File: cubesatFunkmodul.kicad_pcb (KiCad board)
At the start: 4 copper layers, 85 x 85 mm, 214 parts, among them CON11 DISCO-CON1, CON21 DISCO-CON2, Q1 SSM3J334RLFTR-ND, Q10 AO3414, Q11 MMBT5551-TP, Q12 MMBT5551-TP, Q13 MMBT5551-TP, Q14 MMBT5551-TP, Q15 MMBT5551-TP, Q16 MMBT5551-TP, Q17 AO3414, Q18 AO3414, Q2 AO3414, Q3 MMBT5551-TP, Q4 MMBT5551-TP, Q5 MMBT5551-TP, Q6 MMBT5551-TP, Q7 MMBT5551-TP, Q8 MMBT5551-TP, Q9 SSM3J334RLFTR-ND, U1 MC74HC4538A, U10 RFM23BP, U2 MAX892, U3 ATMEGA128-16AU, U4 LTC3113, U5 RFM23BP, U6 MC74HC4538A, U7 MAX892, U8 ATMEGA128-16AU, U9 LTC3113, Y1 Crystal_GND24, Y2 Crystal_GND24

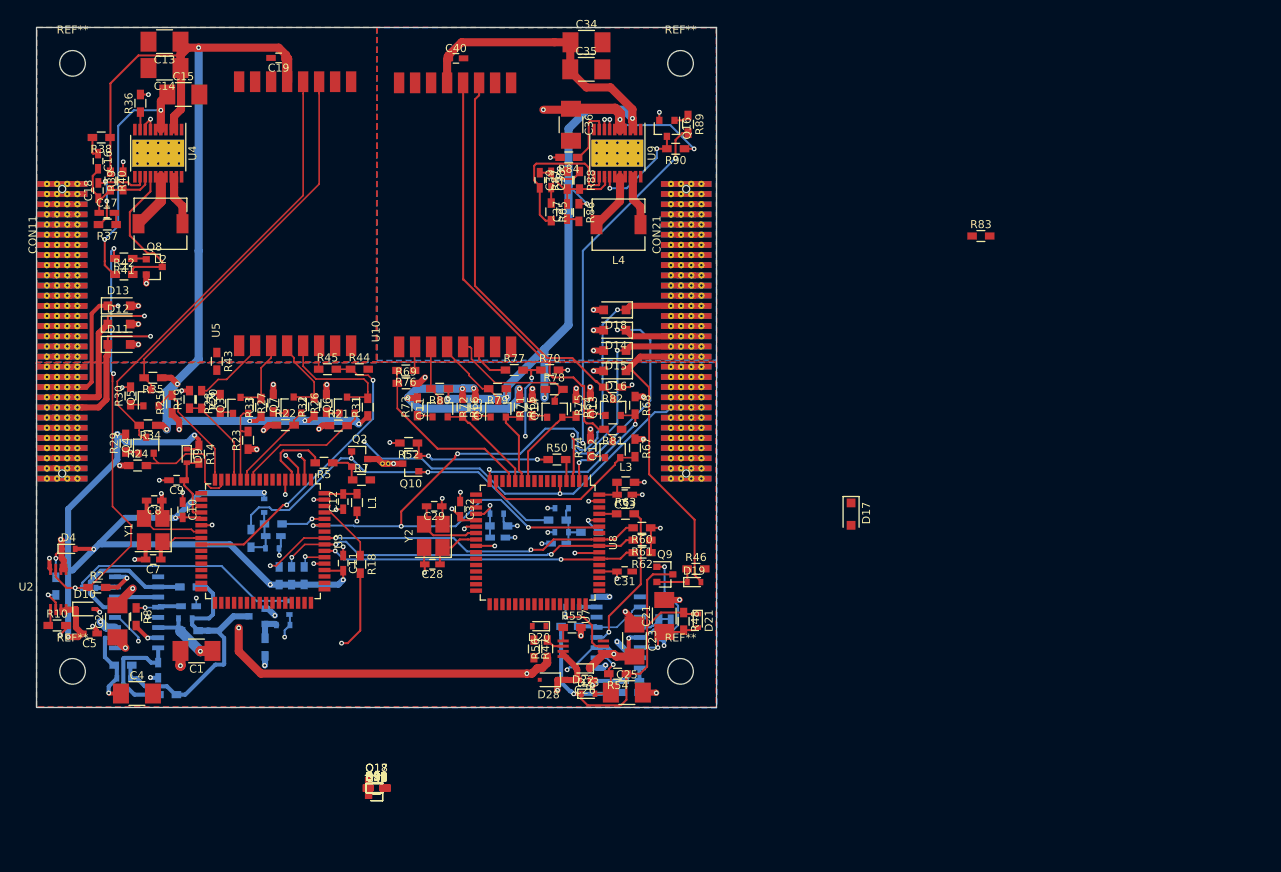
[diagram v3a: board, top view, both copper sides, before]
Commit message: Moved rf module to bottom layer
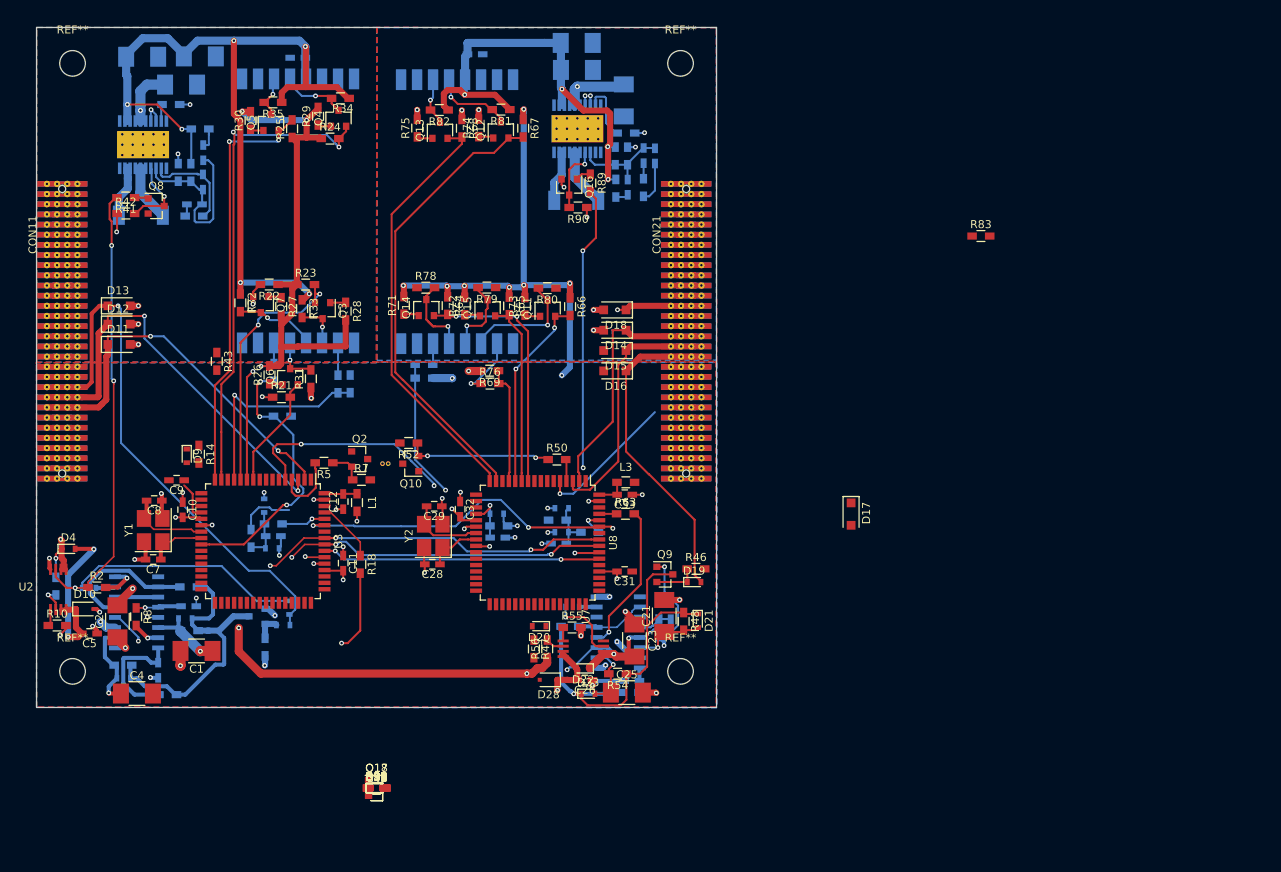
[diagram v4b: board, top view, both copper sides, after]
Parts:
- removed R15, R16, R17, R60, R61, R62: 100k, Resistors_SMD:R_0603_HandSoldering
- C13, C14, C15, C16, C17, C18, C19, C34, C35, C36, C37, C38, C39, C40, L2, L4, R19, R20, R36, R37, R38, R39, R40, R44, R45, R70, R77, R84, R85, R86, R87, R88, U10, U4, U5, U9: moved to B.Cu
- moved Q4 47.4 mm to (88.7, 45.4)
- moved R24 47.4 mm to (87.7, 47.9)
- moved R29 47.4 mm to (86.2, 45.1)
- moved R34 47.4 mm to (89.0, 42.9)
- moved Q12 42.3 mm to (109.0, 46.8)
- moved R67 42.3 mm to (111.8, 46.6)
- moved R81 42.3 mm to (109.1, 44.3)
- moved R74 42.3 mm to (106.3, 46.5)
- moved R75 40.8 mm to (98.6, 46.6)
- moved R82 40.8 mm to (101.3, 44.3)
- moved R68 40.8 mm to (104.2, 46.6)
- moved Q13 40.8 mm to (101.4, 46.9)
- moved R25 37.5 mm to (82.9, 46.7)
- moved Q5 37.5 mm to (80.3, 45.9)
- moved R30 37.5 mm to (77.8, 45.6)
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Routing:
- net /Funkmodul2/Funkeinheit2/5V: track 122.9 -> 56.1 mm, vias 7 -> 4
- net /Funkmodul1/Funkeinheit/5V: track 178.9 -> 124.6 mm, vias 6 -> 7
- net /Funkmodul1/Funkeinheit/RXON_: track 56.0 -> 8.43 mm, vias 0 -> 1
- net VBAT: track 105.1 -> 59.7 mm, vias 5 -> 4
- net /Funkmodul2/Funkeinheit2/RXON_: track 55.3 -> 10.1 mm, vias 0 -> 1
- net /Funkmodul1/Funkeinheit/RXON: track 16.0 -> 61.1 mm, vias 0 -> 2
- net /Funkmodul1/Funkeinheit/TXON_: track 49.4 -> 5.35 mm, vias 0 -> 1
- net /Funkmodul1/VCC: track 139.8 -> 96.6 mm, vias 18 -> 10
- net /Funkmodul2/Funkeinheit2/TXON_: track 48.9 -> 5.96 mm, vias 0 -> 1
- net WIRE_CONN: track 47.5 -> 7.10 mm, vias 2 -> 0
- net /Funkmodul1/Funkeinheit/TXON: track 15.0 -> 52.7 mm, vias 0 -> 2
- net /Funkmodul2/Funkeinheit2/RXON: track 21.3 -> 57.4 mm
- net /Funkmodul2/VCC: track 71.3 -> 101.2 mm, vias 17 -> 16
- net /Funkmodul2/Funkeinheit2/TXON: track 25.4 -> 53.6 mm, vias 2 -> 0
- net /Funkmodul1/Funkeinheit/MOSI: track 10.1 -> 32.8 mm, vias 0 -> 2
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
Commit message: Adds second burnwire fets
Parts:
- removed the REF** at (94.2, 88.5)
- removed the REF** at (95.0, 88.5)
- added D33: SMF3.3, Diodes_SMD:D_SOD-123F, F.Cu at (92.8, 83.7)
- C41, C42, D29, D30, D31, D32, R92, R93, R94, R96, R97, R98: moved to B.Cu
- moved D17 58.3 mm to (94.8, 89.1)
- moved R83 56.1 mm to (115.2, 75.7), turned to 270 degrees
- moved R95 48.5 mm to (95.8, 80.7)
- moved R96 47.2 mm to (95.8, 82.0), turned to 90 degrees
- moved Q17 45.9 mm to (89.7, 83.3)
- moved Q18 45.9 mm to (95.8, 83.3), turned to 180 degrees
- moved R91 45.5 mm to (85.5, 84.3), turned to 180 degrees
- moved R92 44.8 mm to (91.5, 84.3)
- moved R98 40.6 mm to (120.4, 98.7), turned to 180 degrees
- moved D31 39.5 mm to (120.5, 100.2), turned to 180 degrees
- moved D32 38.5 mm to (120.5, 101.6)
- moved C42 36.6 mm to (118.3, 102.1), turned to 270 degrees
- moved R97 34.7 mm to (115.4, 102.1), turned to 180 degrees
- moved R94 28.3 mm to (84.5, 102.3)
- moved C41 26.2 mm to (86.5, 103.8)
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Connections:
- CON21 pad 5: /Funkmodul1/TDI -> /Funkmodul2/TDI
- CON21 pad 6: /Funkmodul2/TDO -> /Funkmodul1/TDO
- R91 pad 2: /Funkmodul1/BURNWIRE -> /Funkmodul1/BURNWIRE2
- R95 pad 2: /Funkmodul2/BURNWIRE -> /Funkmodul2/BURNWIRE2
- U3 pad 55: /Funkmodul2/TDI -> /Funkmodul1/TDO
- U3 pad 6: (no net) -> /Funkmodul1/BURNWIRE2
- U8 pad 55: /Funkmodul2/TDO -> /Funkmodul1/TDI
- U8 pad 6: (no net) -> /Funkmodul2/BURNWIRE2
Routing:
- net /Funkmodul1/TDO: track 0.00 -> 85.1 mm, vias 0 -> 1
- net WIRE_CONN2: track 0.00 -> 60.3 mm, vias 0 -> 1
- net /Funkmodul2/TDO: track 56.6 -> 0.00 mm, vias 1 -> 0
- net VBAT: track 59.7 -> 114.1 mm, vias 4 -> 5
- net WIRE_CONN: track 7.10 -> 49.8 mm, vias 0 -> 2
- net /Funkmodul2/Funkeinheit2/5V: track 56.1 -> 92.5 mm
- net /Funkmodul1/TDI: track 71.7 -> 38.6 mm, vias 1 -> 2
- net /Connector/TCK: track 119.8 -> 89.2 mm, vias 3 -> 4
- net /Funkmodul2/BURNWIRE2: track 0.00 -> 29.6 mm, vias 0 -> 2
- net /Connector/~ENABLE2~: track 40.5 -> 66.4 mm, vias 0 -> 2
- net /Connector/TMS: track 114.4 -> 88.5 mm, vias 3 -> 4
- net /Funkmodul2/TDI: track 34.8 -> 52.6 mm, vias 2 -> 1
- net Net-(U6-Pad11): track 0.00 -> 9.84 mm
- net Net-(C39-Pad2): track 5.11 -> 14.7 mm, vias 0 -> 2
- net GND: track 92.8 -> 101.8 mm, vias 52 -> 57
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
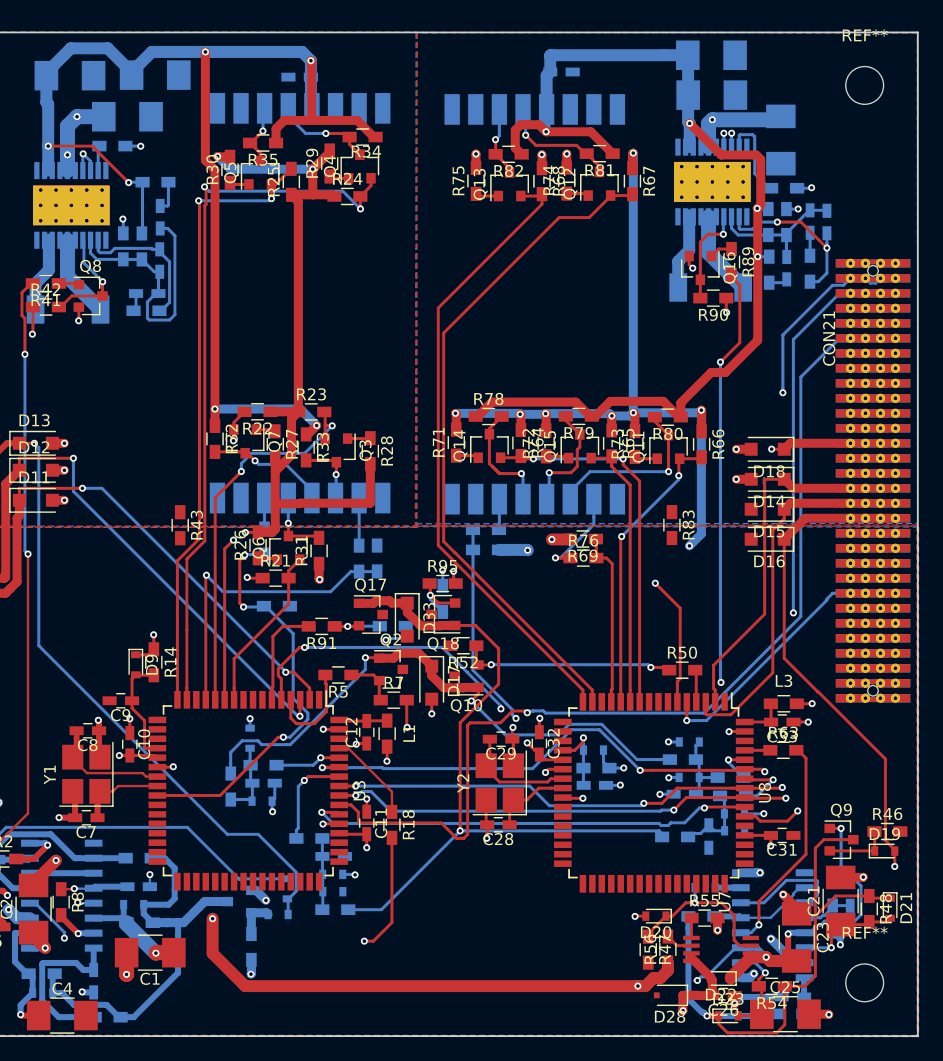
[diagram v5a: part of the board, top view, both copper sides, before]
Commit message: Fixes some drc violations
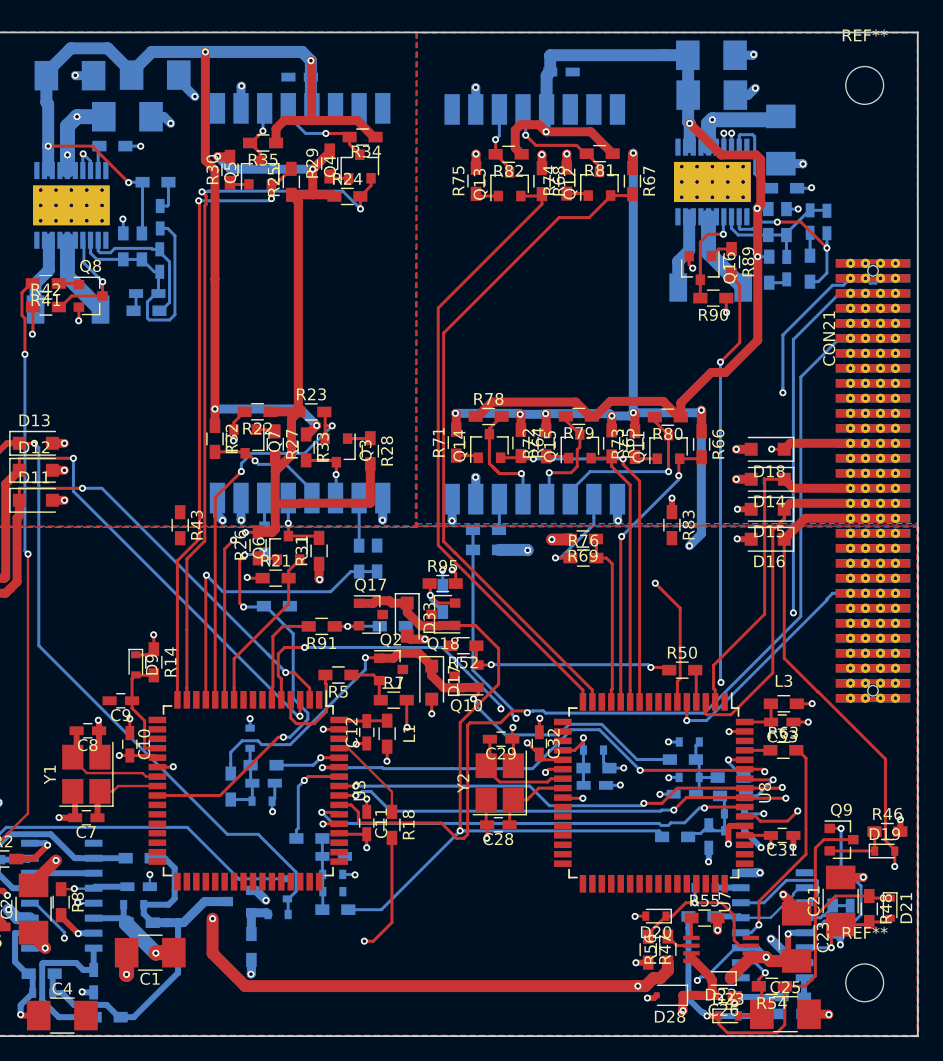
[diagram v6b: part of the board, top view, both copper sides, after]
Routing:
- net /Funkmodul2/Funkeinheit2/PGND: track 0.00 -> 14.0 mm, vias 0 -> 8
- net /Funkmodul1/Funkeinheit/PGND: track 0.00 -> 13.6 mm, vias 0 -> 7
- net GND: track 101.8 -> 114.2 mm, vias 57 -> 65
- net /Connector/~RBF~: track 62.3 -> 63.0 mm
